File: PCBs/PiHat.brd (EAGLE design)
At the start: 65 x 56.5 mm, 20 parts, among them IC1 TPS77030

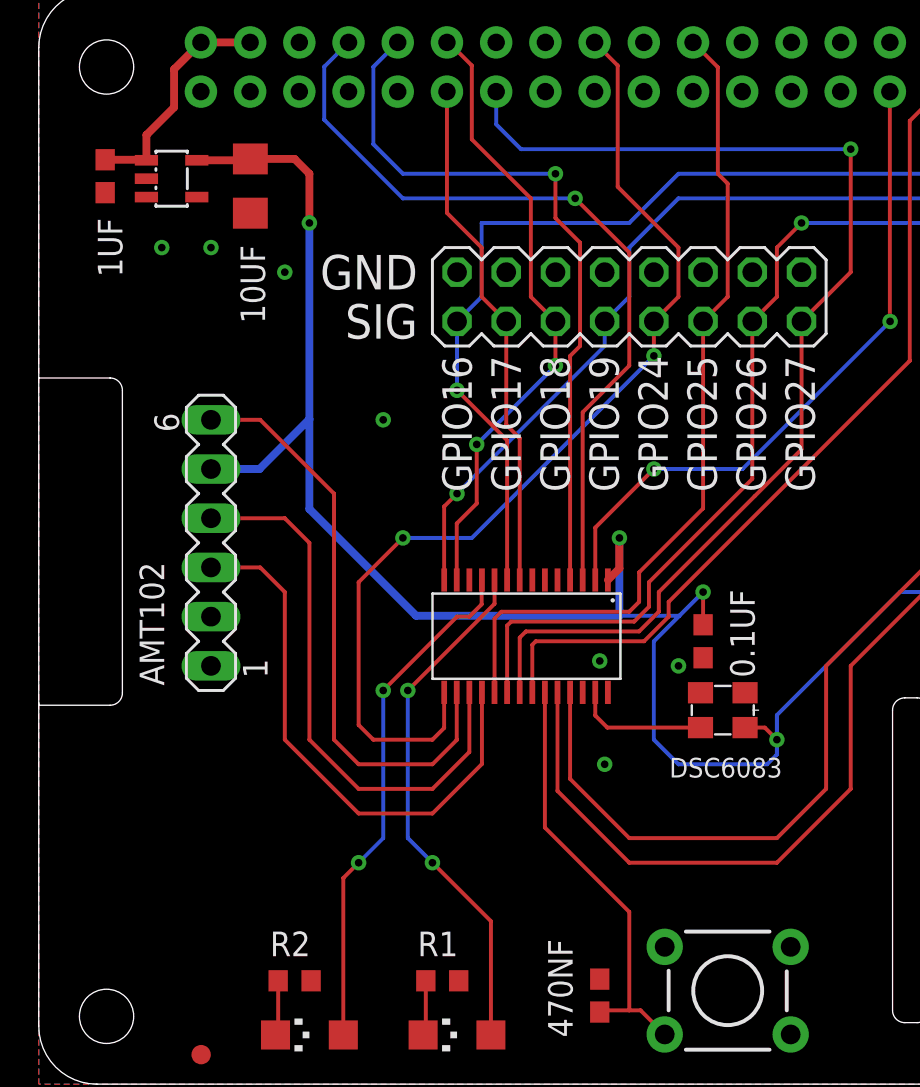
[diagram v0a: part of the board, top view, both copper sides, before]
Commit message: Updated board after debugging first revision
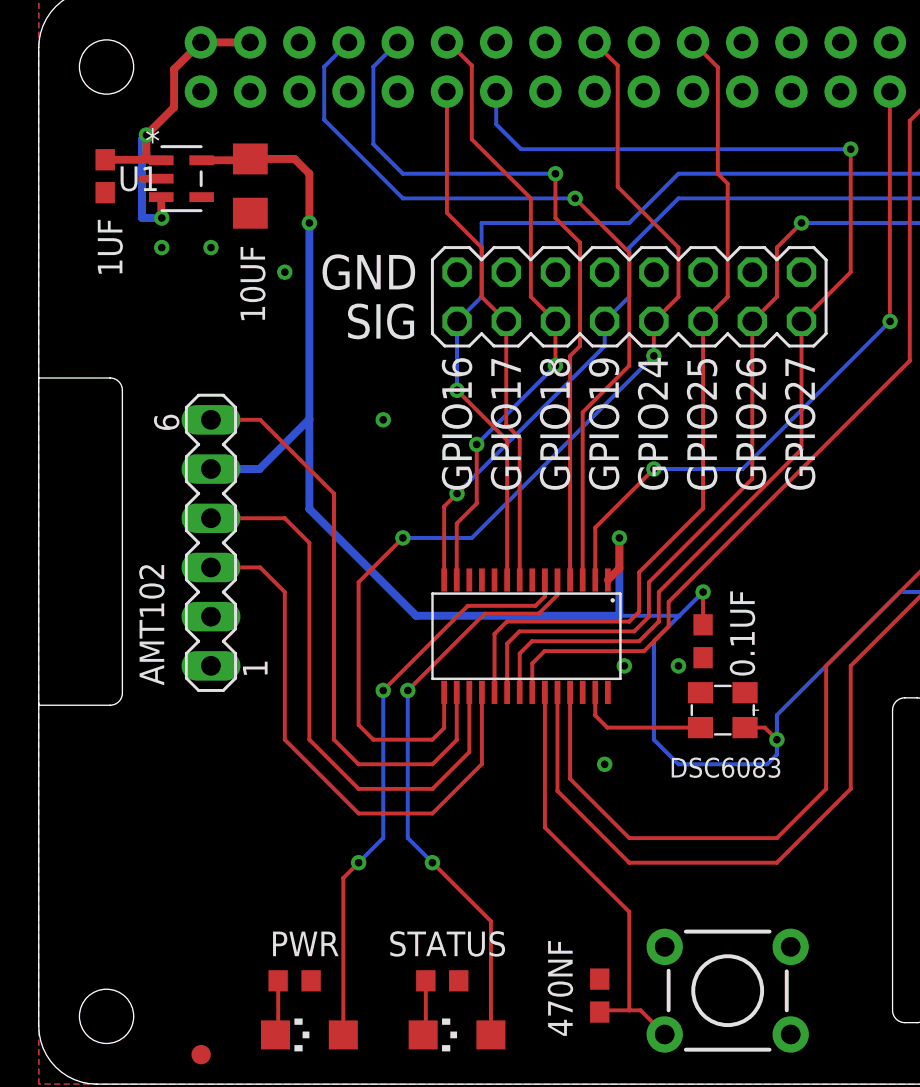
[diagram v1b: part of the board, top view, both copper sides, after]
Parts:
- removed IC1: TPS77030, texas:SOT23-DBV
- added U1: TLV70036DDCTDDC5-L, TLV70036:DDC5-L
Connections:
- net 5.0V: now also U1.1, U1.3; no longer IC1.1
- net GND: now also U1.2; no longer IC1.2, IC1.3
- net LED0: now also U$1.5; no longer U$1.10
- net LED1: now also U$1.6; no longer U$1.11
- net VDD: now also U1.5; no longer IC1.5
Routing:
- net 5.0V: track 11.9 -> 19.3 mm, vias 0 -> 2
- net LED1: track 26.8 -> 29.8 mm
- net LED0: track 27.1 -> 30.1 mm
- net GND: track 0.00 -> 0.99 mm
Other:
- board text added: "PWR"
- board text added: "STATUS"

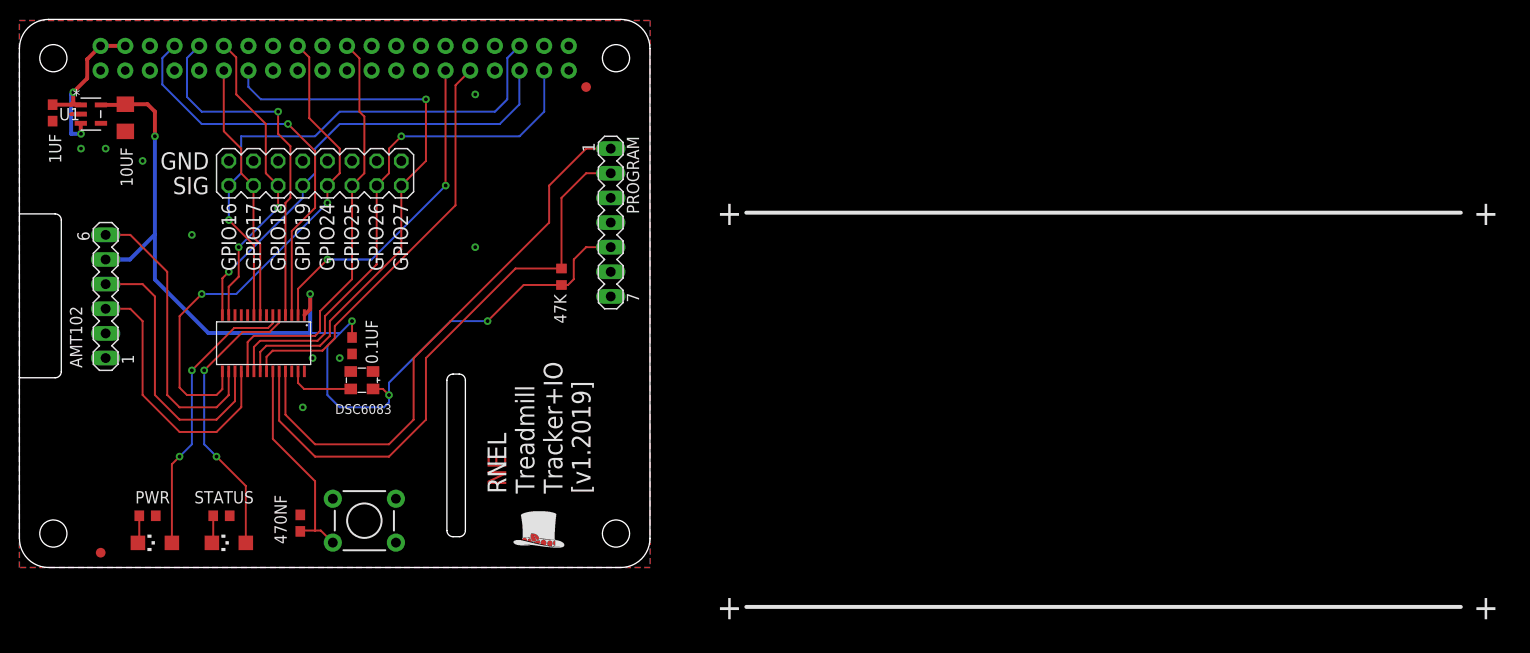
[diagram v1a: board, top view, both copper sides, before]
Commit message: Updated code some more trying to get 2kHz clock to work
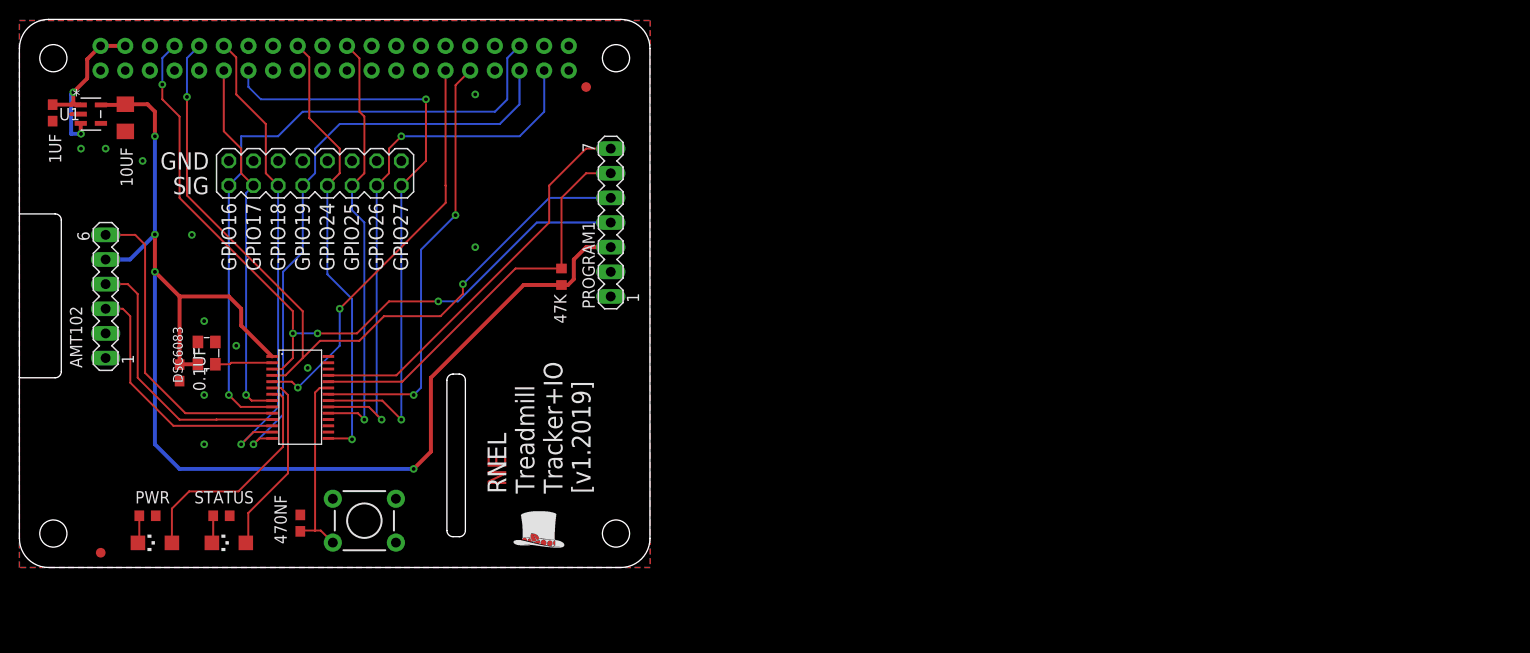
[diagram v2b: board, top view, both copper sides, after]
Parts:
- moved 0.1UF 18.0 mm to (16.5, 20.1)
- moved DSC6083 16.2 mm to (19.3, 22.1), turned to 90 degrees
- moved U$1 6.76 mm to (29.0, 17.5), turned to 270 degrees
- turned PROGRAM1 to 90 degrees
- renumbered PROGRAM to PROGRAM1
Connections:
- removed net INCLK: DSC6083.3, U$1.27
- removed net N$4: U$1.12
- removed net RXD: PROGRAM1.4
- removed net TXD: PROGRAM1.3
- new net TA0CLK: DSC6083.1, U$1.2
- net 5V: now also PROGRAM1.2; no longer PROGRAM1.6
- net GND: now also PROGRAM1.1; no longer PROGRAM1.7
- net GPIO5: now also U$1.5; no longer U$1.2
- net LED0: now also U$1.6; no longer U$1.5
- net LED1: now also U$1.7; no longer U$1.6
- net MSP_RXD: now also PROGRAM1.4
- net MSP_TXD: now also PROGRAM1.5
- net QUAD_A: now also U$1.11; no longer U$1.17
- net QUAD_B: now also U$1.10; no longer U$1.16
- net QUAD_Z: now also U$1.12; no longer U$1.18
- net SBWTCK: now also PROGRAM1.7; no longer PROGRAM1.1
- net SBWTDIO: now also PROGRAM1.6; no longer PROGRAM1.2
- net VDD: now also PROGRAM1.3; no longer PROGRAM1.5
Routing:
- net MSP_TXD: track 37.5 -> 80.7 mm, vias 1 -> 2
- net MSP_RXD: track 41.0 -> 78.4 mm, vias 1 -> 4
- net VDD: track 108.4 -> 135.2 mm, vias 5 -> 4
- net SBWTDIO: track 60.9 -> 42.3 mm
- net SBWTCK: track 57.8 -> 41.0 mm
- net GPIO18: track 32.2 -> 48.7 mm, vias 2 -> 1
- net GPIO19: track 47.6 -> 61.7 mm
- net GPIO16: track 55.1 -> 67.2 mm
- net GPIO17: track 26.8 -> 38.0 mm, vias 0 -> 1
- net LED0: track 30.1 -> 19.0 mm, vias 2 -> 0
- net GPIO5: track 34.2 -> 41.9 mm
- net INCLK: track 6.88 -> 0.00 mm
- net GPIO24: track 52.8 -> 46.4 mm, vias 2 -> 1
- net TA0CLK: track 0.00 -> 5.91 mm
- net LED1: track 29.8 -> 24.3 mm, vias 2 -> 0
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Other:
- board text removed: "+"

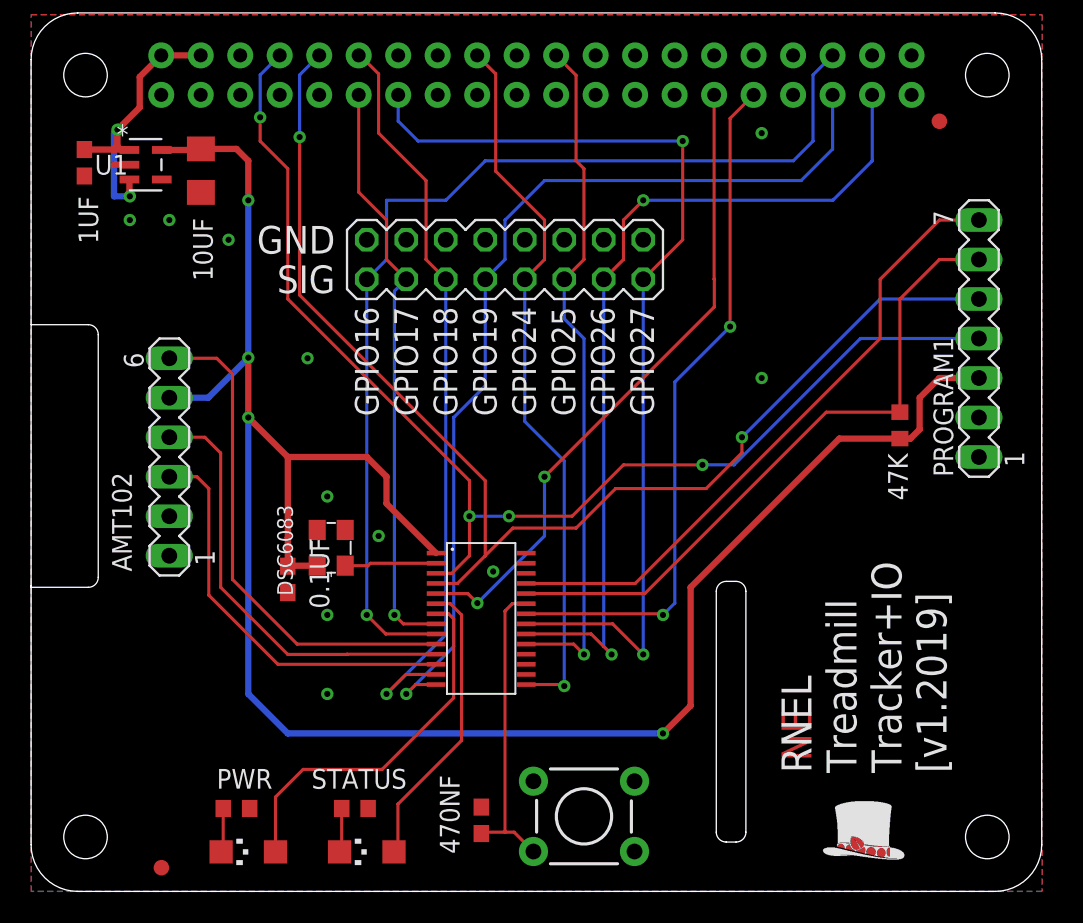
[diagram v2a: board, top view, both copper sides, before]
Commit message: Fixed errors and added a FT230 USB/UART Interface to PCB
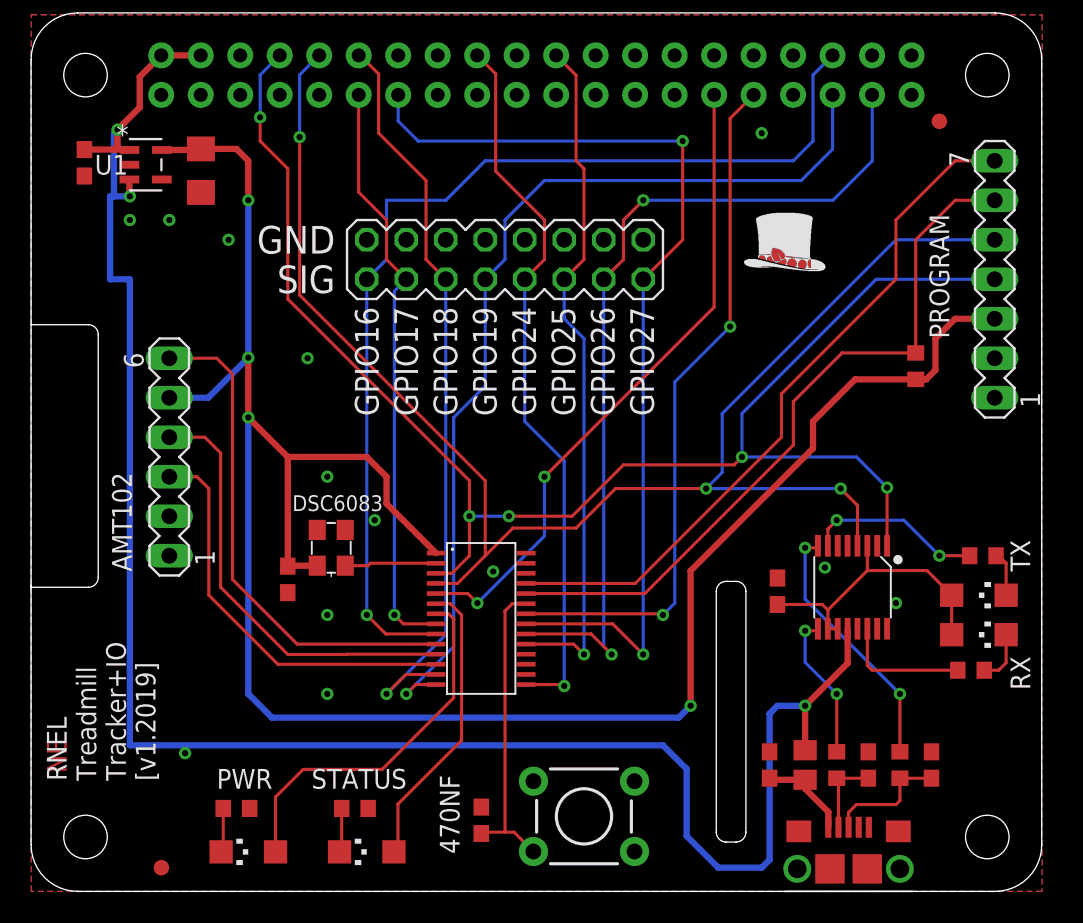
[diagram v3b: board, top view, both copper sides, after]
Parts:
- removed PROGRAM1: (no value), con-lstb-mod:MA07-1
- added C3: 10nF, resistor:C0603
- added C4: 100nF, resistor:C0603
- added C5, C6: 47pF, resistor:C0603
- added FERRITE: (no value), rcl:R0805
- added PROGRAM: (no value), con-lstb-mod:MA07-1
- added R3, R4: 27R, resistor:R0603
- added R5, R6: 300, resistor:R0603
- added RX, TX: (no value), led:CHIPLED_1206
- added U2: FT230, OPL_IC:SSOP16-0.635-5X4MM
- added USB1: MICRO-USB-FCI-10118193, microftx:FCI-10118193-0001LF
- DSC6083: value DSC6083CI2A-002K000-ND -> 2KHZ
- R1, R2: value 300 -> R
- U$1: value G2XX3---PW28 -> MSP430
- moved U$2 38.2 mm to (45.8, 39.9)
- moved 47K 3.94 mm to (56.9, 33.8)
- renumbered 0.1UF to C
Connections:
- new net N$10: R5.1, TX.C
- new net N$3: C3.1, FERRITE.1, USB1.1
- new net N$4: C5.1, R3.1, USB1.2
- new net N$5: R3.2, U2.9
- new net N$7: C6.1, R4.1, USB1.3
- new net N$8: R4.2, U2.8
- new net N$9: R6.1, RX.C
- new net RXLED: R6.2, U2.14
- new net TXLED: R5.2, U2.7
- new net VCCIO: C4.1, RX.A, TX.A, U2.10, U2.11, U2.3
- net 5.0V: now also FERRITE.2, U2.12
- net 5V: now also PROGRAM.2; no longer PROGRAM1.2
- net GND: now also C3.2, C4.2, C5.2, C6.2, PROGRAM.1, U2.13, U2.5, USB1.5, USB1.G1, USB1.G2, USB1.G3, USB1.G4, USB1.G5, USB1.G6; no longer PROGRAM1.1
- net MSP_RXD: now also PROGRAM.4, U2.1; no longer PROGRAM1.4
- net MSP_TXD: now also PROGRAM.5, U2.4; no longer PROGRAM1.5
- net SBWTCK: now also PROGRAM.7; no longer PROGRAM1.7
- net SBWTDIO: now also PROGRAM.6; no longer PROGRAM1.6
- net VDD: now also PROGRAM.3; no longer PROGRAM1.3
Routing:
- net 5.0V: track 19.3 -> 124.1 mm, vias 2 -> 3
- net VCCIO: track 0.00 -> 19.0 mm
- net MSP_RXD: track 78.4 -> 96.5 mm, vias 4 -> 5
- net MSP_TXD: track 80.7 -> 97.7 mm, vias 2 -> 3
- net N$8: track 0.00 -> 16.5 mm, vias 0 -> 2
- net TXLED: track 0.00 -> 11.4 mm, vias 0 -> 2
- net N$5: track 0.00 -> 9.51 mm, vias 0 -> 2
- net RXLED: track 0.00 -> 8.30 mm
- net N$7: track 0.00 -> 8.04 mm
- net N$3: track 0.00 -> 6.00 mm
- net N$4: track 0.00 -> 5.23 mm
- net SBWTDIO: track 42.3 -> 46.5 mm
- net SBWTCK: track 41.0 -> 45.3 mm
- net N$9: track 0.00 -> 3.41 mm
- net VDD: track 135.2 -> 138.5 mm
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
